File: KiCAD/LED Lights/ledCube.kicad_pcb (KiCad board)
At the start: 2 copper layers, 52 x 22 mm, 14 parts, among them P1 CONN_01X03, P2 CONN_01X02, P3 CONN_01X02, P4 CONN_01X02, P5 CONN_01X02, U1 AL8805W5

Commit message: clean up
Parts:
- P1: value CONN_01X03 -> Power
- P2, P4: value CONN_01X02 -> LED +VE
- P3, P5: value CONN_01X02 -> LED -VE
- R3: moved to F.Cu
- moved R3 3.96 mm to (137.2, 105.2), turned to 0 degrees
- moved L1 1.04 mm to (136.1, 99.6)
- turned P2 to 90 degrees
- turned P4 to 90 degrees
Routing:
- net /LED+/U: track 15.9 -> 18.5 mm
- net /LED+/L: track 16.4 -> 13.8 mm
- net /PWM: track 18.1 -> 17.5 mm, vias 1 -> 0
- net GND: track 15.4 -> 14.8 mm, vias 13 -> 9
- added copper zone on F.Cu, net GND
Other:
- board text added: "LedCube v.0"
- board text removed: "BlueSink LedCube v.0"

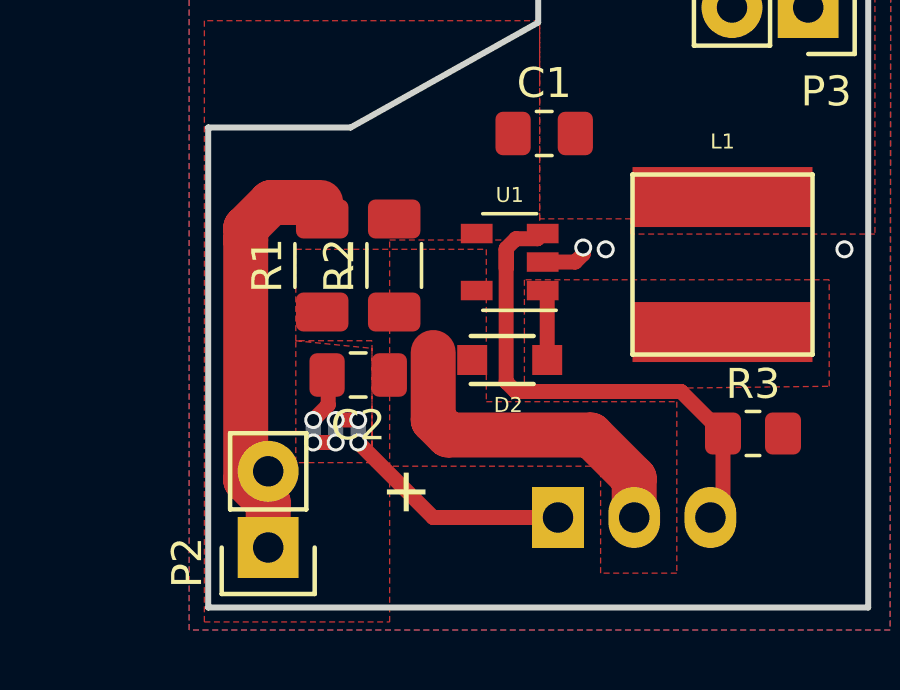
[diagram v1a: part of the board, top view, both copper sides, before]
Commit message: removal of vias
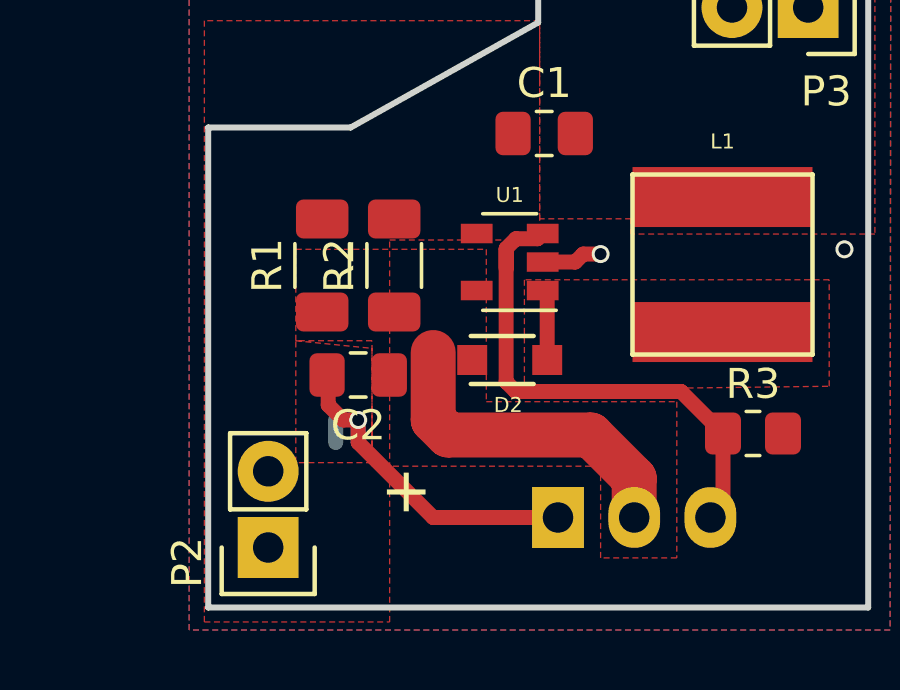
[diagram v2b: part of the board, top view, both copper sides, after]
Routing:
- net /LED+/L: track 13.8 -> 0.00 mm
- net GND: track 14.8 -> 14.2 mm, vias 9 -> 3
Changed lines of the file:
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@@
 	)
 	(segment
-		(start 123.25 104.75)
+		(start 123 103.25)
+		(end 123 104.25)
+		(width 0.5)
+		(layer "F.Cu")
+		(net 2)
+	)
+	(segment
+		(start 123.5 104.75)
 		(end 124 104.75)
 		(width 0.5)
@@
 	)
 	(segment
-		(start 130.15 99.484286)
-		(end 131.234286 99.484286)
-		(width 0.5)
-		(layer "F.Cu")
-		(net 2)
-	)
-	(segment
-		(start 123 103.25)
-		(end 123 104.25)
+		(start 123 104.25)
+		(end 123.5 104.75)
 		(width 0.5)
 		(layer "F.Cu")
@@
 	)
 	(segment
+		(start 132.08 99.218572)
+		(end 131.5 99.218572)
+		(width 0.5)
+		(layer "F.Cu")
+		(net 2)
+	)
+	(segment
 		(start 131.234286 99.484286)
-		(end 131.5 99.218572)
-		(width 0.5)
-		(layer "F.Cu")
-		(net 2)
-	)
-	(segment
-		(start 123 104.25)
-		(end 122.5 104.75)
+		(end 130.15 99.484286)
+		(width 0.5)
+		(layer "F.Cu")
+		(net 2)
+	)
+	(segment
+		(start 124 104.75)
+		(end 124 105.5)
 		(width 0.5)
 		(layer "F.Cu")
@@
 	(segment
 		(start 131.5 99.218572)
-		(end 131.5 99)
-		(width 0.5)
-		(layer "F.Cu")
-		(net 2)
-	)
-	(segment
-		(start 122.5 105.5)
-		(end 123.25 105.5)
+		(end 131.234286 99.484286)
 		(width 0.5)
 		(layer "F.Cu")
@@
 	)
 	(via
-		(at 132.25 99.06)
-		(size 0.6)
-		(drill 0.4)
-		(layers "F.Cu" "B.Cu")
-		(net 2)
-	)
-	(via
-		(at 122.5 104.75)
-		(size 0.6)
-		(drill 0.4)
-		(layers "F.Cu" "B.Cu")
-		(net 2)
-	)
-	(via
-		(at 124 105.5)
-		(size 0.6)
-		(drill 0.4)
-		(layers "F.Cu" "B.Cu")
-		(net 2)
-	)
-	(via
-		(at 122.5 105.5)
-		(size 0.6)
-		(drill 0.4)
-		(layers "F.Cu" "B.Cu")
-		(net 2)
-	)
-	(via
 		(at 124 104.75)
 		(size 0.6)
@@
 	)
 	(via
-		(at 131.5 99)
+		(at 132.08 99.218572)
 		(size 0.6)
 		(drill 0.4)
@@
 		(net 2)
 	)
-	(via
-		(at 123.25 104.75)
-		(size 0.6)
-		(drill 0.4)
-		(layers "F.Cu" "B.Cu")
-		(net 2)
-	)
-	(via
-		(at 123.25 105.5)
-		(size 0.6)
-		(drill 0.4)
-		(layers "F.Cu" "B.Cu")
-		(net 2)
-	)
 	(segment
 		(start 124 104.75)
@@
 	)
 	(segment
-		(start 122.5 104.75)
-		(end 122.5 105.5)
-		(width 0.5)
-		(layer "B.Cu")
-		(net 2)
-	)
-	(segment
 		(start 129.256714 98.708286)
 		(end 129.976 98.708286)
@@
 		(layer "B.Cu")
 		(net 4)
-	)
-	(segment
-		(start 121 107.5)
-		(end 120.25 106.75)
-		(width 1.5)
-		(layer "F.Cu")
-		(net 5)
-	)
-	(segment
-		(start 120.25 98.35)
-		(end 121.1 97.5)
-		(width 1.5)
-		(layer "F.Cu")
-		(net 5)
-	)
-	(segment
-		(start 121.1 97.5)
-		(end 122.75 97.5)
-		(width 1.5)
-		(layer "F.Cu")
-		(net 5)
-	)
-	(segment
-		(start 121 109)
-		(end 121 107.5)
-		(width 1.5)
-		(layer "F.Cu")
-		(net 5)
-	)
-	(segment
-		(start 120.25 106.75)
-		(end 120.25 98.75)
-		(width 1.5)
-		(layer "F.Cu")
-		(net 5)
-	)
-	(segment
-		(start 120.25 98.75)
-		(end 120.25 98.35)
-		(width 1.5)
-		(layer "F.Cu")
-		(net 5)
 	)
 	(segment
@@
 		(polygon
 			(pts
-				(xy 121.92 99.06) (xy 126.365 99.06) (xy 128.27 99.06) (xy 128.27 104.14) (xy 134.62 104.14) (xy 134.62 109.855)
-				(xy 132.08 109.855) (xy 132.08 106.29) (xy 124.46 106.29) (xy 124.46 102.108) (xy 121.92 102.108)
-			)
-		)
+				(xy 121.92 99.06) (xy 126.365 99.06) (xy 128.27 99.06) (xy 128.27 104.14) (xy 134.62 104.14) (xy 134.62 109.347)
+				(xy 132.08 109.347) (xy 132.08 106.29) (xy 124.46 106.29) (xy 124.46 102.108) (xy 121.92 102.108)
+			)
+		)
